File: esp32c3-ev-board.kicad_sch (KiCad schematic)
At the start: 65 parts, among them IC1 SPX3819M5-L-3-3, IC2 ACS711EEXTK-31AB-T, IC3 ESP32-C3FH4, IC4 W25Q128JVSIQ, J1 Battery Neg(Series), J2 Battery Pos, J3 Barrel_Jack, J4 Conn_01x04_Pin, J5 USB_C_Receptacle_USB2.0, SW1 SW_DPST_x2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

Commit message: shape and placement nearly finished, doing perephirals next
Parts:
- added R15: 1k, Resistor_SMD:R_0805_2012Metric_Pad1.20x1.40mm_HandSolder, symbol Device:R
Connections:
- net +3.3V: now also R15.2; no longer D1.2 (A)
- new net: D1.2 (A), R15.1
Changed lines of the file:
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@@
+    (stroke (width 0) (type default))
+  )
+  (wire (pts (xy 387.35 83.82) (xy 387.35 86.36))
     (stroke (width 0) (type default))
   )
@@
   )
   (wire (pts (xy 351.79 226.06) (xy 359.41 226.06))
-    (stroke (width 0) (type default))
-  )
-  (wire (pts (xy 387.35 76.2) (xy 387.35 86.36))
     (stroke (width 0) (type default))
   )
@@
         )
       )
+    )
+  )
+  (symbol (lib_id "Device:R") (at 387.35 80.01 180) (unit 1)
+    (in_bom yes) (on_board yes) (dnp no) (fields_autoplaced)
+    (property "Reference" "R15" (at 389.89 78.74 0)
+      (effects (font (size 1.27 1.27)) (justify right))
+    )
+    (property "Value" "1k" (at 389.89 81.28 0)
+      (effects (font (size 1.27 1.27)) (justify right))
+    )
+    (property "Footprint" "Resistor_SMD:R_0805_2012Metric_Pad1.20x1.40mm_HandSolder" (at 389.128 80.01 90)
+      (effects (font (size 1.27 1.27)) hide)
+    )
+    (property "Datasheet" "~" (at 387.35 80.01 0)
+      (effects (font (size 1.27 1.27)) hide)
+    )
+    (pin "1")
+    (pin "2")
+    (instances
+      (project "esp32c3-ev-board"
+        (path "/f5da1fcc-93b5-4c63-bb34-c18c11bc243c"
+          (reference "R15") (unit 1)
+        )
+      )

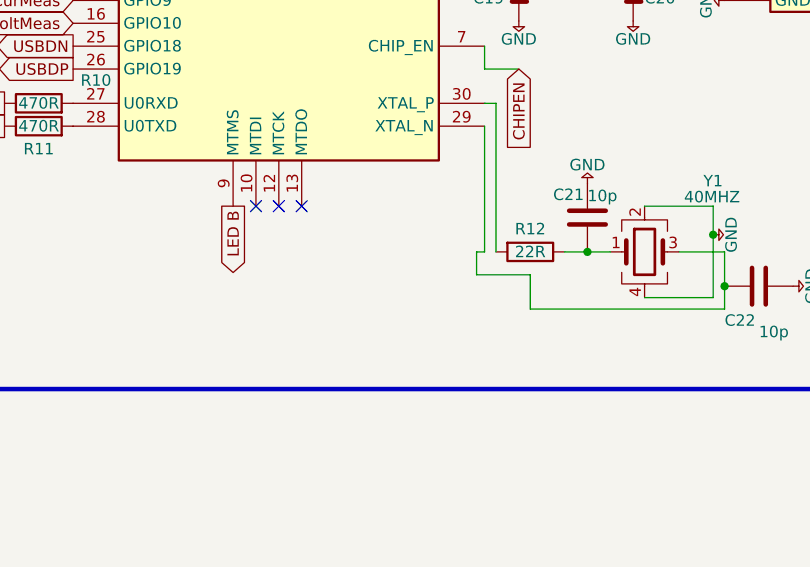
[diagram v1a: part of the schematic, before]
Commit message: almost completed board layout
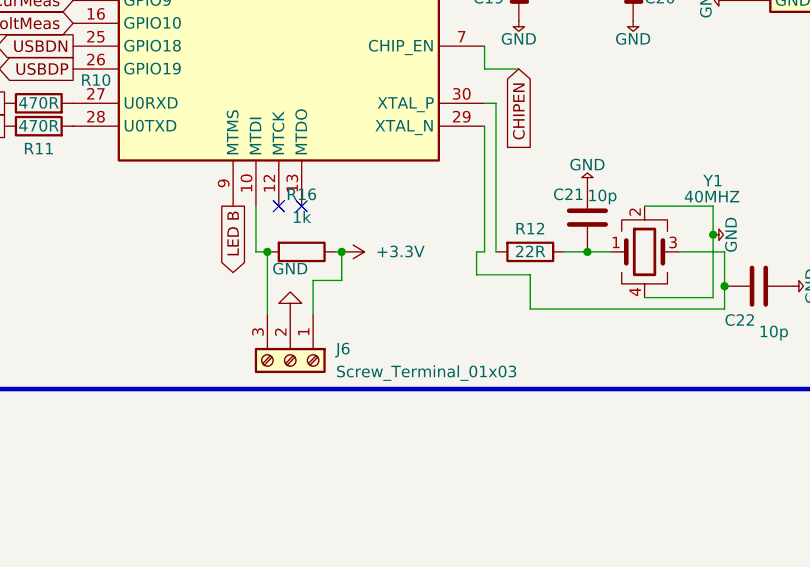
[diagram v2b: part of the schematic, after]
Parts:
- added J6: Screw_Terminal_01x03, Connector_PinSocket_2.54mm:PinSocket_1x03_P2.54mm_Vertical, symbol Connector:Screw_Terminal_01x03
- added R16: 1k, Resistor_SMD:R_0805_2012Metric_Pad1.20x1.40mm_HandSolder, symbol Device:R
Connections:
- net +3.3V: now also J6.1 (Pin_1), R16.1
- net GND: now also J6.2 (Pin_2)
- net at IC3.10 (MTDI): now also J6.3 (Pin_3), R16.2
- no-connect marks 12 -> 11
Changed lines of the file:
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@@
   (junction (at 334.01 76.2) (diameter 0) (color 0 0 0 0)
   )
+  (junction (at 318.135 231.14) (diameter 0) (color 0 0 0 0)
+  )
   (junction (at 151.13 245.11) (diameter 0) (color 0 0 0 0)
   )
@@
   (junction (at 132.08 265.43) (diameter 0) (color 0 0 0 0)
   )
+  (junction (at 309.88 231.14) (diameter 0) (color 0 0 0 0)
+  )
   (junction (at 314.96 83.82) (diameter 0) (color 0 0 0 0)
   )
@@
   )
   (no_connect (at 181.61 91.44))
-  (no_connect (at 313.69 226.06))
   (no_connect (at 181.61 86.36))
   (no_connect (at 151.13 237.49))
+  (no_connect (at 313.69 226.06))
   (no_connect (at 288.29 187.96))
   (no_connect (at 181.61 88.9))
   (no_connect (at 173.99 227.33))
   (no_connect (at 151.13 234.95))
-  (no_connect (at 308.61 226.06))
   (no_connect (at 288.29 185.42))
   (no_connect (at 181.61 83.82))
@@
     (stroke (width 0) (type default))
   )
+  (wire (pts (xy 314.96 234.315) (xy 318.135 234.315))
+    (stroke (width 0) (type default))
+  )
   (wire (pts (xy 334.01 231.14) (xy 334.01 217.17))
     (stroke (width 0) (type default))
@@
     (stroke (width 0) (type default))
   )
+  (wire (pts (xy 314.96 238.125) (xy 314.96 234.315))
+    (stroke (width 0) (type default))
+  )
   (wire (pts (xy 360.68 231.14) (xy 360.68 234.95))
     (stroke (width 0) (type default))
@@
     (stroke (width 0) (type default))
   )
+  (wire (pts (xy 317.5 231.14) (xy 318.135 231.14))
+    (stroke (width 0) (type default))
+  )
   (wire (pts (xy 152.4 88.9) (xy 153.67 88.9))
     (stroke (width 0) (type default))
   )
+  (wire (pts (xy 308.61 231.14) (xy 308.61 226.06))
+    (stroke (width 0) (type default))
+  )
   (wire (pts (xy 166.37 66.04) (xy 166.37 68.58))
     (stroke (width 0) (type default))
@@
     (stroke (width 0) (type default))
   )
+  (wire (pts (xy 309.88 238.125) (xy 309.88 231.14))
+    (stroke (width 0) (type default))
+  )
   (wire (pts (xy 334.01 190.5) (xy 360.68 190.5))
     (stroke (width 0) (type default))
@@
     (stroke (width 0) (type default))
   )
+  (wire (pts (xy 309.88 231.14) (xy 308.61 231.14))
+    (stroke (width 0) (type default))
+  )
   (wire (pts (xy 157.48 66.04) (xy 166.37 66.04))
     (stroke (width 0) (type default))
@@
   )
   (wire (pts (xy 162.56 71.12) (xy 163.83 71.12))
+    (stroke (width 0) (type default))
+  )
+  (wire (pts (xy 318.135 234.315) (xy 318.135 231.14))
     (stroke (width 0) (type default))
   )
@@
     )
   )
+  (symbol (lib_id "power:GND") (at 312.42 238.125 180) (unit 1)
+    (in_bom yes) (on_board yes) (dnp no) (fields_autoplaced)
+    (property "Reference" "#PWR037" (at 312.42 231.775 0)
+      (effects (font (size 1.27 1.27)) hide)
+    )
+    (property "Value" "GND" (at 312.42 233.045 0)
+      (effects (font (size 1.27 1.27)))
+    )
+    (property "Footprint" "" (at 312.42 238.125 0)
+      (effects (font (size 1.27 1.27)) hide)
+    )
+    (property "Datasheet" "" (at 312.42 238.125 0)
+      (effects (font (size 1.27 1.27)) hide)
+    )
+    (pin "1")
+    (instances
+      (project "esp32c3-ev-board"
+        (path "/f5da1fcc-93b5-4c63-bb34-c18c11bc243c"
+          (reference "#PWR037") (unit 1)
+        )
+      )
+    )
+  )
   (symbol (lib_id "power:+3.3V") (at 55.88 184.15 0) (unit 1)
     (in_bom yes) (on_board yes) (dnp no) (fields_autoplaced)
@@
         (path "/f5da1fcc-93b5-4c63-bb34-c18c11bc243c"
           (reference "J1") (unit 1)
+        )
+      )
+    )
+  )
+  (symbol (lib_id "Device:R") (at 313.69 231.14 270) (unit 1)
+    (in_bom yes) (on_board yes) (dnp no) (fields_autoplaced)
+    (property "Reference" "R16" (at 313.69 224.79 90)
+      (effects (font (size 1.27 1.27)))
+    )
+    (property "Value" "1k" (at 313.69 227.33 90)
+      (effects (font (size 1.27 1.27)))
+    )
+    (property "Footprint" "Resistor_SMD:R_0805_2012Metric_Pad1.20x1.40mm_HandSolder" (at 313.69 229.362 90)
+      (effects (font (size 1.27 1.27)) hide)
+    )
+    (property "Datasheet" "~" (at 313.69 231.14 0)
+      (effects (font (size 1.27 1.27)) hide)
+    )
+    (pin "1")
+    (pin "2")
+    (instances
+      (project "esp32c3-ev-board"
+        (path "/f5da1fcc-93b5-4c63-bb34-c18c11bc243c"
+          (reference "R16") (unit 1)
         )
       )
@@
     )
   )
+  (symbol (lib_id "Connector:Screw_Terminal_01x03") (at 312.42 243.205 270) (unit 1)
+    (in_bom yes) (on_board yes) (dnp no) (fields_autoplaced)
+    (property "Reference" "J6" (at 317.5 241.935 90)
+      (effects (font (size 1.27 1.27)) (justify left))
+    )
+    (property "Value" "Screw_Terminal_01x03" (at 317.5 244.475 90)
+      (effects (font (size 1.27 1.27)) (justify left))
+    )
+    (property "Footprint" "Connector_PinSocket_2.54mm:PinSocket_1x03_P2.54mm_Vertical" (at 312.42 243.205 0)
+      (effects (font (size 1.27 1.27)) hide)
+    )
+    (property "Datasheet" "~" (at 312.42 243.205 0)
+      (effects (font (size 1.27 1.27)) hide)
+    )
+    (pin "1")
+    (pin "2")
+    (pin "3")
+    (instances
+      (project "esp32c3-ev-board"
+        (path "/f5da1fcc-93b5-4c63-bb34-c18c11bc243c"
+          (reference "J6") (unit 1)
+        )
+      )
+    )
+  )
   (symbol (lib_name "+3.3V_1") (lib_id "power:+3.3V") (at 382.27 76.2 0) (unit 1)
     (in_bom yes) (on_board yes) (dnp no) (fields_autoplaced)
@@
         )
       )
+    )
+  )
+  (symbol (lib_id "power:+3.3V") (at 318.135 231.14 270) (unit 1)
+    (in_bom yes) (on_board yes) (dnp no) (fields_autoplaced)
+    (property "Reference" "#PWR038" (at 314.325 231.14 0)
+      (effects (font (size 1.27 1.27)) hide)
+    )
+    (property "Value" "+3.3V" (at 321.945 231.14 90)
+      (effects (font (size 1.27 1.27)) (justify left))
+    )
+    (property "Footprint" "" (at 318.135 231.14 0)
+      (effects (font (size 1.27 1.27)) hide)
+    )
+    (property "Datasheet" "" (at 318.135 231.14 0)
+      (effects (font (size 1.27 1.27)) hide)
+    )
+    (pin "1")
+    (instances
+      (project "esp32c3-ev-board"
+        (path "/f5da1fcc-93b5-4c63-bb34-c18c11bc243c"
+          (reference "#PWR038") (unit 1)
+        )
+      )

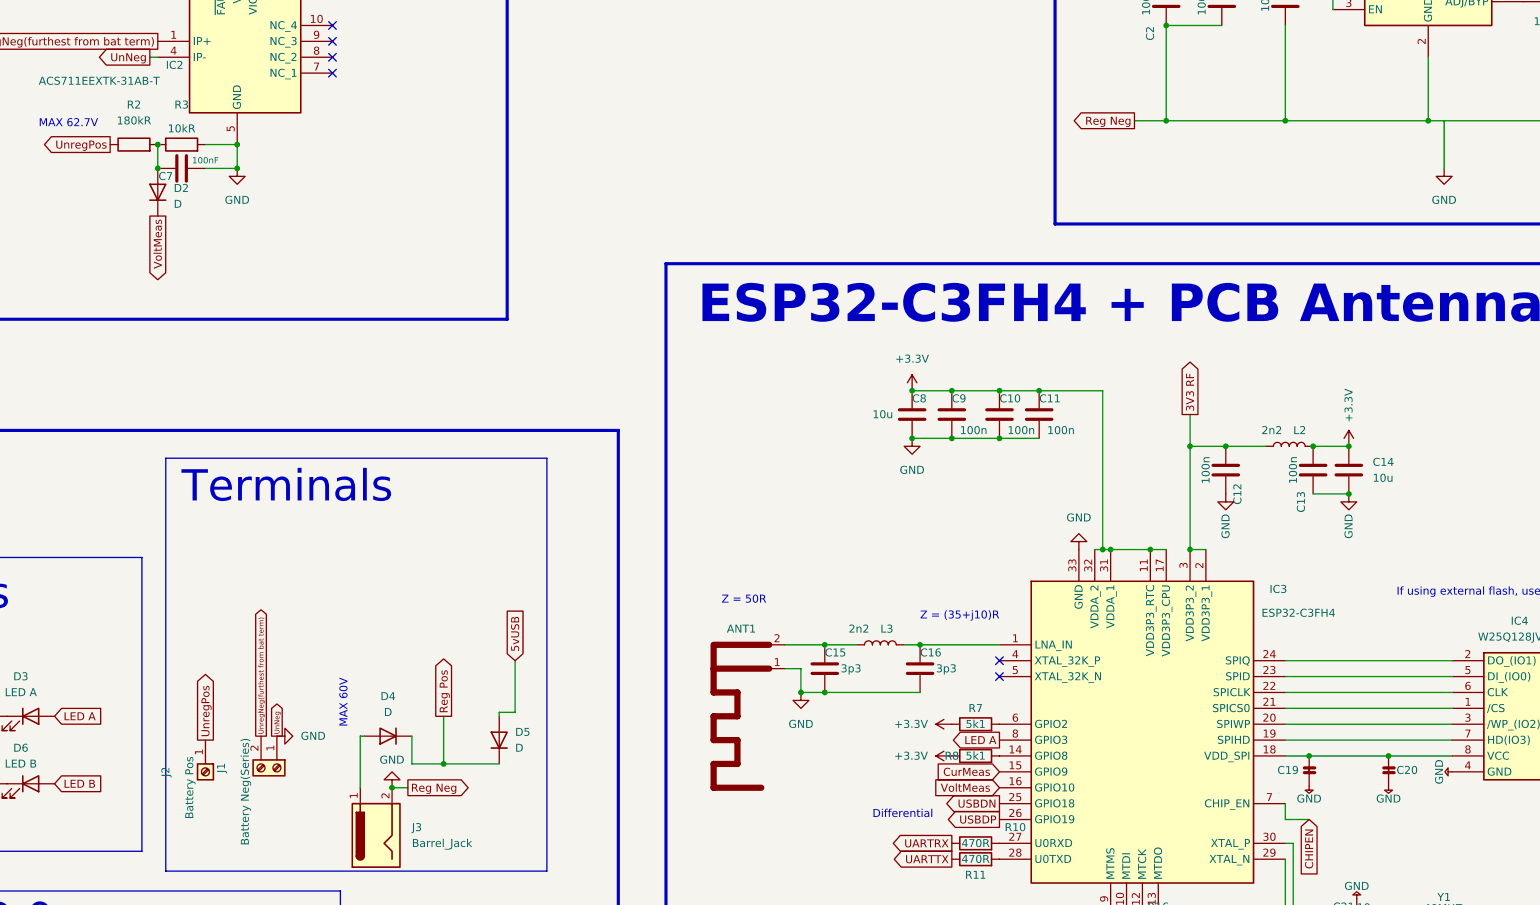
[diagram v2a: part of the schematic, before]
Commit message: starting outline REMEMBER TO ORDER 100k resistor size 0805
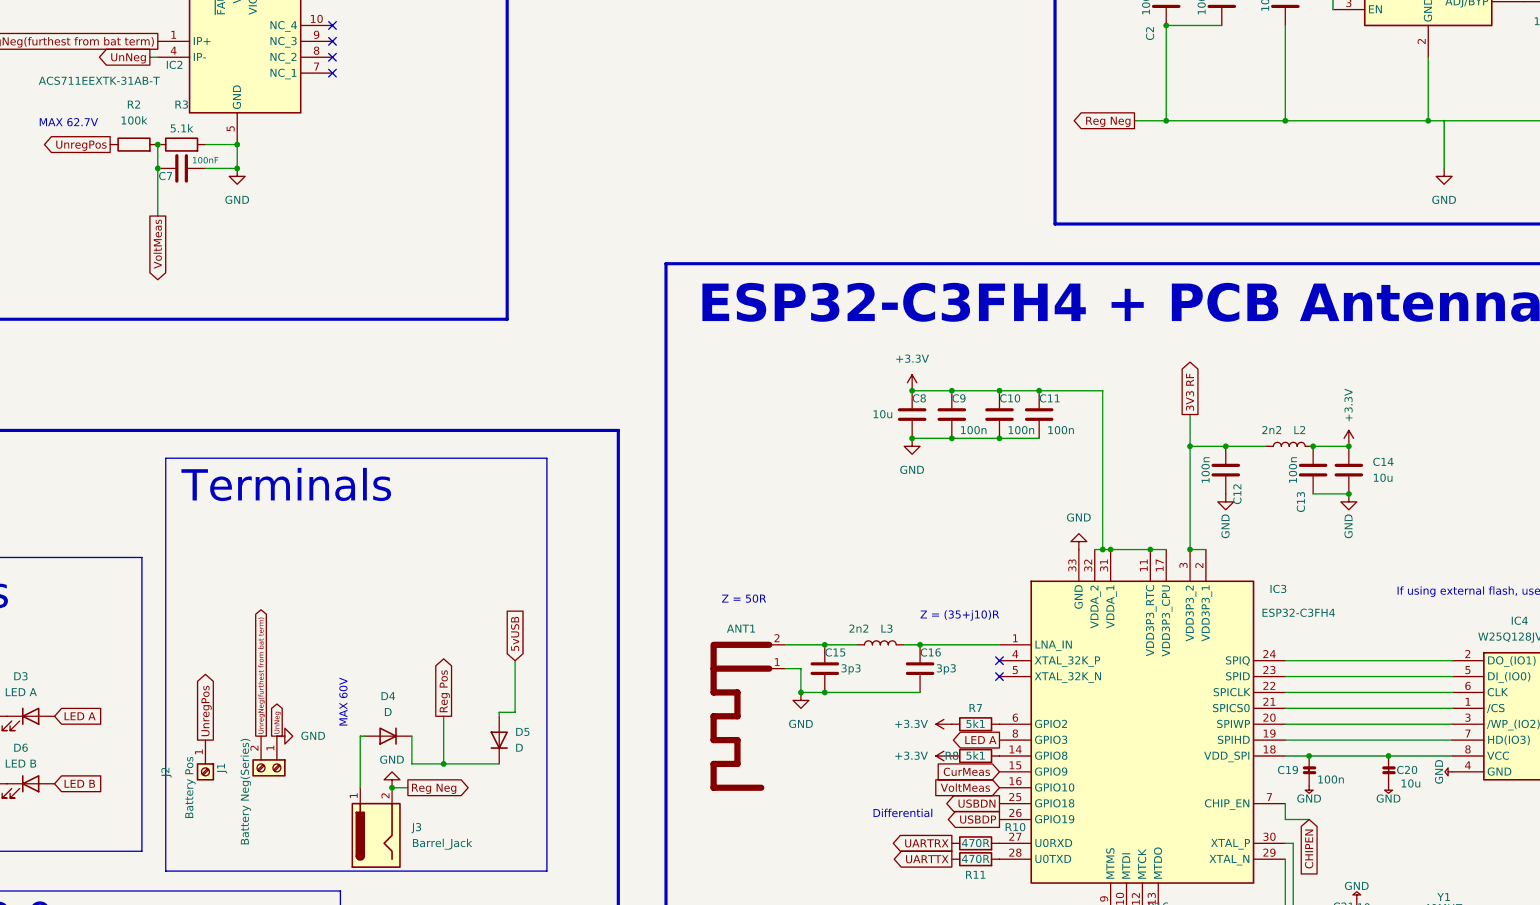
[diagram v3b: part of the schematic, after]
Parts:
- removed D2: D, Diode_SMD:D_SMB_Handsoldering, symbol Device:D
- C19: value C -> 100n
- C20: value C -> 10u
- R2: value 180kR -> 100k; footprint Resistor_THT:R_Axial_DIN0309_L9.0mm_D3.2mm_P12.70mm_Horizontal -> Resistor_SMD:R_0805_2012Metric_Pad1.20x1.40mm_HandSolder
- R3: value 10kR -> 5.1k; footprint Resistor_THT:R_Axial_DIN0309_L9.0mm_D3.2mm_P12.70mm_Horizontal -> Resistor_SMD:R_1206_3216Metric_Pad1.30x1.75mm_HandSolder
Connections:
- net VoltMeas: now also C7.1, R2.2, R3.1
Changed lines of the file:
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@@
   (junction (at 151.13 254) (diameter 0) (color 0 0 0 0)
   )
-  (junction (at 153.67 106.68) (diameter 0) (color 0 0 0 0)
-  )
   (junction (at 334.01 76.2) (diameter 0) (color 0 0 0 0)
   )
@@
   (junction (at 314.96 76.2) (diameter 0) (color 0 0 0 0)
   )
+  (junction (at 153.67 106.68) (diameter 0) (color 0 0 0 0)
+  )
   (junction (at 344.17 151.13) (diameter 0) (color 0 0 0 0)
   )
@@
     (stroke (width 0) (type default))
   )
+  (wire (pts (xy 153.67 106.68) (xy 153.67 114.3))
+    (stroke (width 0) (type default))
+  )
   (wire (pts (xy 312.42 167.64) (xy 314.96 167.64))
     (stroke (width 0) (type default))
@@
     )
   )
-  (symbol (lib_id "Device:D") (at 153.67 110.49 90) (unit 1)
-    (in_bom yes) (on_board yes) (dnp no)
-    (property "Reference" "D2" (at 156.21 109.855 90)
-      (effects (font (size 1.27 1.27)) (justify right))
-    )
-    (property "Value" "D" (at 156.21 112.395 90)
-      (effects (font (size 1.27 1.27)) (justify right))
-    )
-    (property "Footprint" "Diode_SMD:D_SMB_Handsoldering" (at 153.67 110.49 0)
-      (effects (font (size 1.27 1.27)) hide)
-    )
-    (property "Datasheet" "~" (at 153.67 110.49 0)
-      (effects (font (size 1.27 1.27)) hide)
-    )
-    (property "Sim.Device" "D" (at 153.67 110.49 0)
-      (effects (font (size 1.27 1.27)) hide)
-    )
-    (property "Sim.Pins" "1=K 2=A" (at 153.67 110.49 0)
-      (effects (font (size 1.27 1.27)) hide)
-    )
-    (pin "1")
-    (pin "2")
-    (instances
-      (project "esp32c3-ev-board"
-        (path "/f5da1fcc-93b5-4c63-bb34-c18c11bc243c"
-          (reference "D2") (unit 1)
-        )
-      )
-    )
-  )
   (symbol (lib_id "Power_Protection:USBLC6-2SC6") (at 121.92 250.19 270) (unit 1)
     (in_bom yes) (on_board yes) (dnp no)
@@
       (effects (font (size 1.27 1.27)))
     )
-    (property "Value" "180kR" (at 149.86 99.06 90)
+    (property "Value" "100k" (at 149.86 99.06 90)
       (effects (font (size 1.27 1.27)))
     )
-    (property "Footprint" "Resistor_THT:R_Axial_DIN0309_L9.0mm_D3.2mm_P12.70mm_Horizontal" (at 149.86 104.648 90)
+    (property "Footprint" "Resistor_SMD:R_0805_2012Metric_Pad1.20x1.40mm_HandSolder" (at 149.86 104.648 90)
       (effects (font (size 1.27 1.27)) hide)
     )
@@
       (effects (font (size 1.27 1.27)) (justify left))
     )
-    (property "Value" "C" (at 341.63 204.216 0)
-      (effects (font (size 1.27 1.27)) (justify left) hide)
+    (property "Value" "100n" (at 339.09 204.47 0)
+      (effects (font (size 1.27 1.27)) (justify left))
     )
     (property "Footprint" "Capacitor_SMD:C_0603_1608Metric_Pad1.08x0.95mm_HandSolder" (at 338.7852 206.756 0)
@@
       (effects (font (size 1.27 1.27)) (justify left))
     )
-    (property "Value" "C" (at 354.33 204.216 0)
-      (effects (font (size 1.27 1.27)) (justify left) hide)
+    (property "Value" "10u" (at 352.425 205.105 0)
+      (effects (font (size 1.27 1.27)) (justify left))
     )
     (property "Footprint" "Capacitor_SMD:C_0603_1608Metric_Pad1.08x0.95mm_HandSolder" (at 351.4852 206.756 0)
@@
       (effects (font (size 1.27 1.27)))
     )
-    (property "Value" "10kR" (at 157.48 100.33 90)
+    (property "Value" "5.1k" (at 157.48 100.33 90)
       (effects (font (size 1.27 1.27)))
     )
-    (property "Footprint" "Resistor_THT:R_Axial_DIN0309_L9.0mm_D3.2mm_P12.70mm_Horizontal" (at 157.48 104.648 90)
+    (property "Footprint" "Resistor_SMD:R_1206_3216Metric_Pad1.30x1.75mm_HandSolder" (at 157.48 104.648 90)
       (effects (font (size 1.27 1.27)) hide)
     )

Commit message: finished outline
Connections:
- net GND: now also ANT1.2; no longer ANT1.1
- net at C15.1, L3.1: now also ANT1.1; no longer ANT1.2
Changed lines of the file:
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@@
       (effects (font (size 1.27 1.27)) hide)
     )
+    (pin "2")
     (pin "1")
-    (pin "2")
     (instances
       (project "esp32c3-ev-board"

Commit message: Almost finished
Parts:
- removed J1: Battery Neg(Series), symbol Connector:Screw_Terminal_01x02
- removed R16: 1k, Resistor_SMD:R_0805_2012Metric_Pad1.20x1.40mm_HandSolder, symbol Device:R
- added H5, H6: MountingHole_Pad, MountingHole:MountingHole_2.7mm_M2.5_Pad, symbol Mechanical:MountingHole_Pad
- added IC5: AH1390-HK4-7, AH1390-HK4-7:AH1390HK47, symbol AH1390-HK4-7:AH1390-HK4-7
- added J7: Conn_01x04_Pin, Connector_PinHeader_2.54mm:PinHeader_1x04_P2.54mm_Vertical, symbol Connector:Conn_01x04_Pin
- added J9: Battery Neg(Series), Connector_PinSocket_2.54mm:PinSocket_1x02_P2.54mm_Vertical, symbol Connector:Screw_Terminal_01x02
- added R17: 1k, Resistor_SMD:R_0805_2012Metric_Pad1.20x1.40mm_HandSolder, symbol Device:R
- ANT1: footprint Library:antenna -> (none)
- SW1, SW2: footprint FSM2JSMAATR:FSM2J_1 -> SKRPANE010:SKRPADE010
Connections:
- net +3.3V: now also R17.2
- net CHIPEN: now also SW2.2 (B)
- net CurMeas: now also SW1.2 (B)
- net GND: now also J6.3 (Pin_3), SW1.3 (B), SW1.4 (B), SW2.3 (B), SW2.4 (B), H5.1, J9.2 (Pin_2); no longer H2.1, J6.2 (Pin_2), SW1.2 (B), SW2.2 (B)
- net LED B: now also IC3.12 (MTCK); no longer IC3.9 (MTMS)
- net UnregNeg(furthest from bat term): now also H6.1
- net UnregPos: now also H2.1
- net VBUS: now also J4.2 (Pin_2); no longer J4.1 (Pin_1)
- net at C21.1, Y1.1: now also R12.2; no longer R12.1
- net at IC3.10 (MTDI): now also J6.2 (Pin_2); no longer J6.3 (Pin_3)
- net at U2.4 (I/O2): now also J4.1 (Pin_1); no longer J4.2 (Pin_2)
- net at IC3.30 (XTAL_P): now also R12.1; no longer R12.2
- net USBDN renamed USBD-
- net USBDP renamed USBD+
- new net: IC5.1 (VDD), J7.1 (Pin_1)
- new net: IC5.2 (GND), J7.4 (Pin_4)
- new net: IC5.3 (OUTPUT_2_(SOUTH-_POLE)), J7.3 (Pin_3)
- new net: IC5.4 (OUTPUT_1_(NORTH_-POLE), J7.2 (Pin_2)
- new net: IC3.9 (MTMS), J9.1 (Pin_1), R17.1
- no-connect marks 11 -> 10
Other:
- moved on the sheet: R12
